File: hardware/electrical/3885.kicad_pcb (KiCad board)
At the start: 4 copper layers, 33 x 77 mm, 112 parts, among them J1 USB_B_Micro, J2 TC2030, J3 Micro_SD_Card_Det1, J4 JST-PH, J5 FFC, Q1 AO3400A, Q2 AO3400A, Q3 AO3401A, Q4 AO3401A, Q5 2N7002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

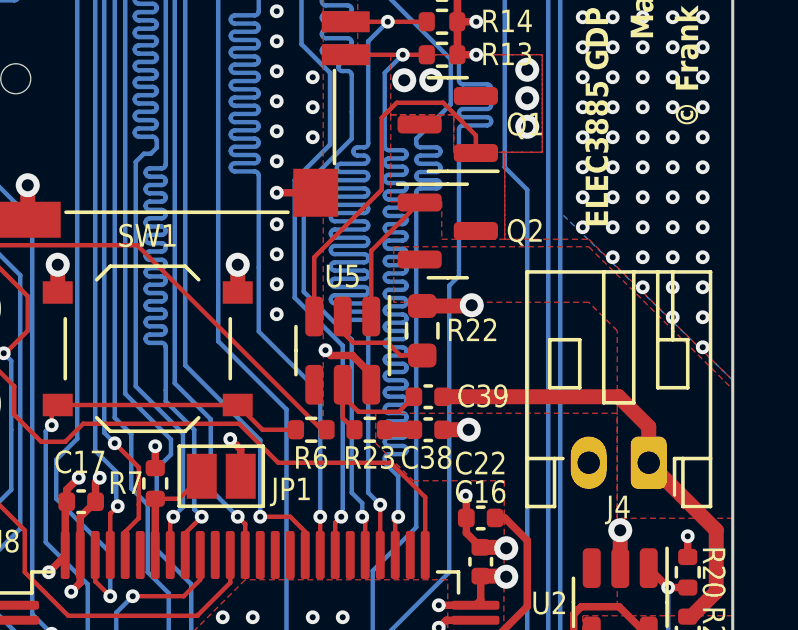
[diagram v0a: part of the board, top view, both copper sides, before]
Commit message: Implement James' recommendations
* Move R22 GND via out of -BATT fill
* Remove TP1 from schematic
* Remove TP2 from schematic
* Remove JP2 from schematic
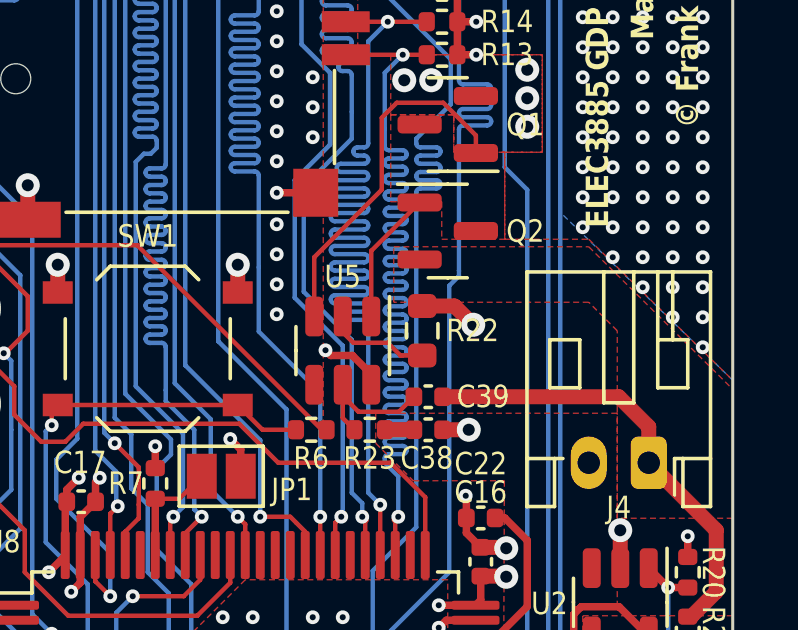
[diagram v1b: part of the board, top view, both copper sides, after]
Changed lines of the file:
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@@
     (property "ki_description" "USB Micro Type B connector")
     (property "ki_keywords" "connector USB micro")
-    (attr smd exclude_from_pos_files exclude_from_bom)
+    (attr smd exclude_from_pos_files)
     (fp_text reference "J1" (at -3.9 2.75 unlocked) (layer "F.SilkS")
         (effects (font (size 0.75 0.65) (thickness 0.12)) (justify right bottom))
@@
     (property "ki_description" "Generic connector, single row, 01x02, script generated")
     (property "ki_keywords" "connector")
-    (attr through_hole exclude_from_pos_files exclude_from_bom)
+    (attr through_hole exclude_from_pos_files)
     (fp_text reference "J4" (at 1 -1.5 unlocked) (layer "F.SilkS")
         (effects (font (size 0.75 0.65) (thickness 0.12)))
@@
     (tags "SMD SMT SPST EVQPUK EVQPUB")
     (property "LCSC Part #" "C2762970")
-    (property "Mfr" "PANASONIC")
+    (property "Mfr" "G-Switch")
     (property "Mfr. Part #" "GT-TC018B-H0375-L1")
     (property "Sheetfile" "mcu.kicad_sch")
@@
   (segment (start 150.95 76.21) (end 151 76.26) (width 0.5) (layer "F.Cu") (net 1))
   (segment (start 143.02 127.45) (end 143.02 129.1) (width 0.5) (layer "F.Cu") (net 1))
-  (segment (start 156.3 102.1) (end 156.275 102.125) (width 0.5) (layer "F.Cu") (net 1))
   (segment (start 136.25 138.16) (end 135.36 138.16) (width 0.5) (layer "F.Cu") (net 1))
   (segment (start 134.89 134.75) (end 134.25 134.75) (width 0.25) (layer "F.Cu") (net 1))
+  (segment (start 155.725 102.125) (end 154.65 102.125) (width 0.5) (layer "F.Cu") (net 1))
   (segment (start 156.12 109.19) (end 156.12 108.47) (width 0.25) (layer "F.Cu") (net 1))
   (segment (start 161.17 131.3) (end 160.3 131.3) (width 0.5) (layer "F.Cu") (net 1))
@@
   (segment (start 161.95 79.75) (end 158.98 79.75) (width 0.5) (layer "F.Cu") (net 1))
   (segment (start 138.27 119.53) (end 138.25 119.55) (width 0.25) (layer "F.Cu") (net 1))
-  (segment (start 156.275 102.125) (end 154.65 102.125) (width 0.5) (layer "F.Cu") (net 1))
   (segment (start 137.82 72.52) (end 137.8 72.5) (width 0.5) (layer "F.Cu") (net 1))
   (segment (start 161.95 76.75) (end 163.04 76.75) (width 0.5) (layer "F.Cu") (net 1))
@@
   (segment (start 143 126.85) (end 143 127.43) (width 0.25) (layer "F.Cu") (net 1))
   (segment (start 151.6 103.775) (end 151.425 103.6) (width 0.25) (layer "F.Cu") (net 1))
+  (segment (start 156.35 102.75) (end 155.725 102.125) (width 0.5) (layer "F.Cu") (net 1))
   (segment (start 138.27 114.6) (end 138.27 113.6) (width 0.25) (layer "F.Cu") (net 1))
   (segment (start 151.4 136.8) (end 150.35 136.8) (width 0.5) (layer "F.Cu") (net 1))
@@
   (via (at 138 89.5) (size 0.46) (drill 0.2) (layers "F.Cu" "B.Cu") (net 1))
   (via (at 149 112.5) (size 0.46) (drill 0.2) (layers "F.Cu" "B.Cu") (net 1))
-  (via (at 156.3 102.1) (size 0.8) (drill 0.4) (layers "F.Cu" "B.Cu") (net 1))
+  (via (at 156.35 102.75) (size 0.8) (drill 0.4) (layers "F.Cu" "B.Cu") (net 1))
   (via (at 157.25 138.65) (size 0.8) (drill 0.4) (layers "F.Cu" "B.Cu") (net 1))
   (via (at 154 79.5) (size 0.46) (drill 0.2) (layers "F.Cu" "B.Cu") (net 1))

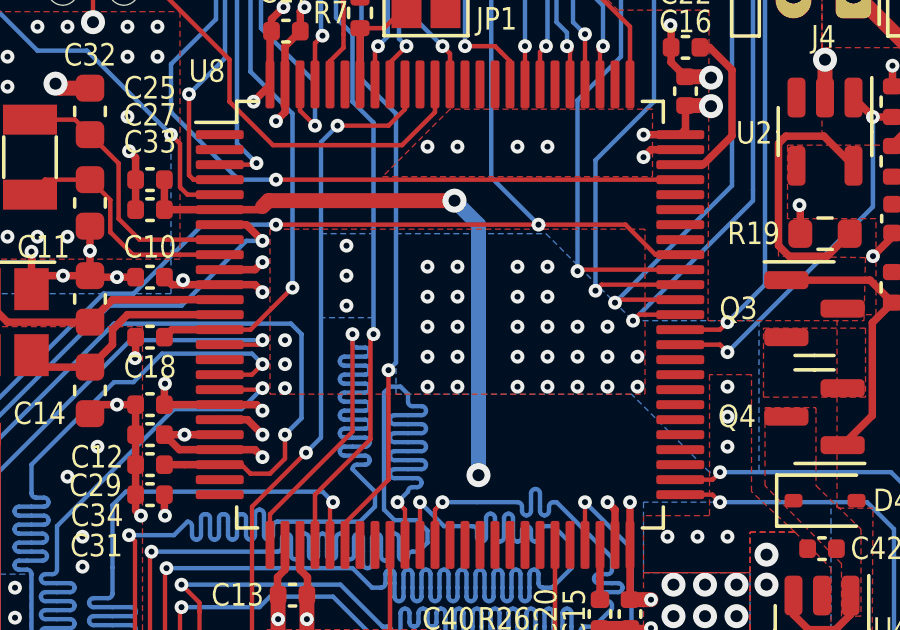
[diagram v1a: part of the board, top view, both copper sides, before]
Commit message: Add JLCPCB order number location
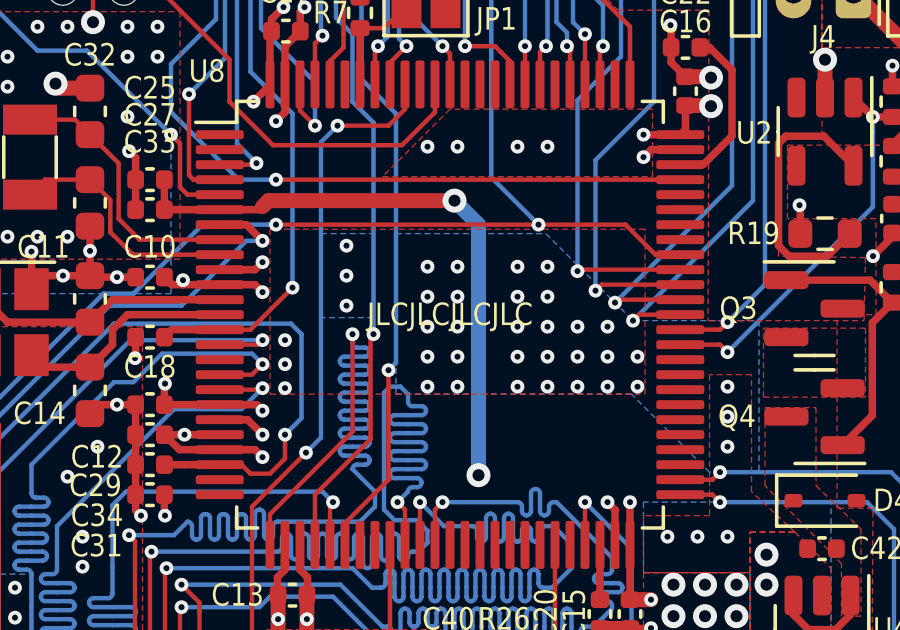
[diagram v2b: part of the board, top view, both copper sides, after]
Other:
- board text added: "JLCJLCJLCJLC"
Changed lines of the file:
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@@
   (gr_line (start 162.5 143.5) (end 134.5 143.5)
     (stroke (width 0.1) (type default)) (layer "Edge.Cuts"))
+  (gr_text "JLCJLCJLCJLC" (at 148.75 118.1) (layer "F.SilkS")
+    (effects (font (size 0.75 0.65) (thickness 0.12)))
+  )
   (gr_text "© Frank Plowman 2023" (at 163.5 84.45 90) (layer "F.SilkS")
     (effects (font (size 0.75 0.65) (thickness 0.12) bold) (justify right))

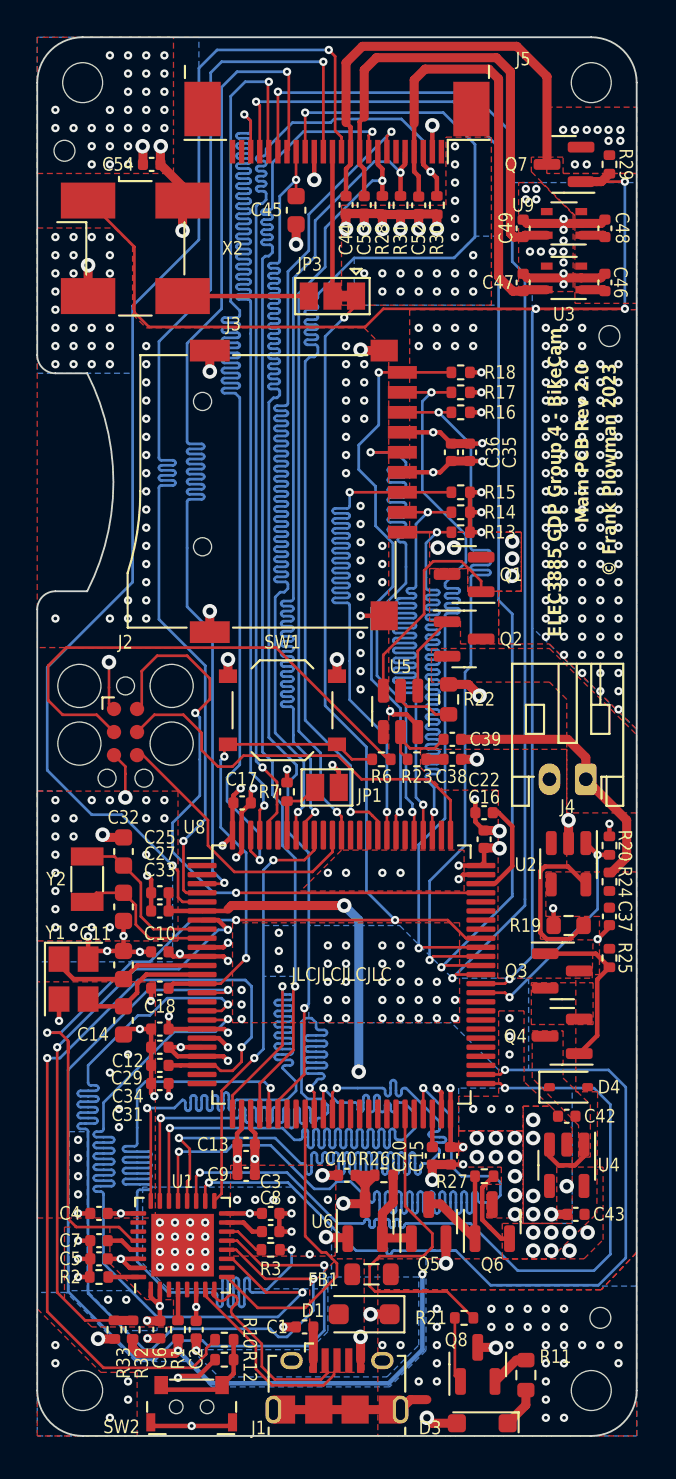
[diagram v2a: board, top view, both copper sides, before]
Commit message: Adjust part positions and rotations to match JLCPCB
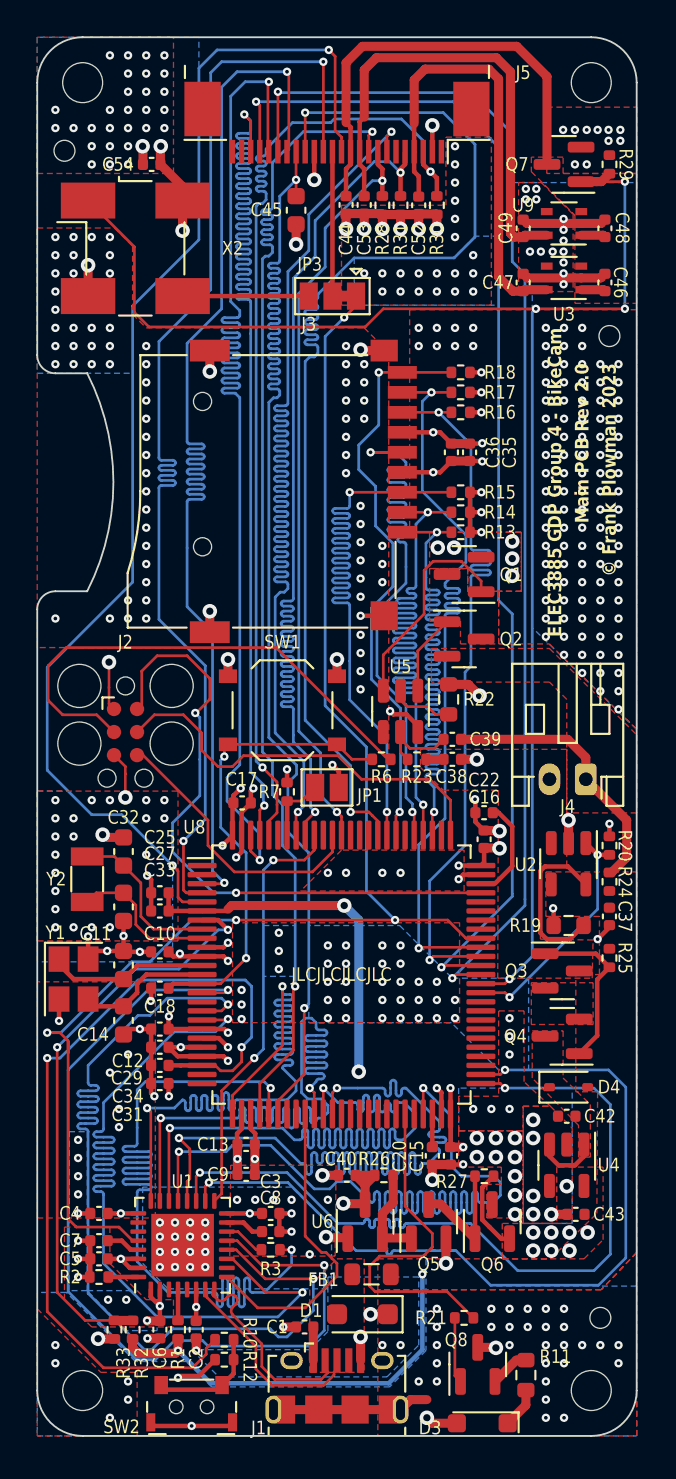
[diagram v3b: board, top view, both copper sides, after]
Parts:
- moved J3 4.15 mm to (146.9, 91.5)
- moved J5 0.75 mm to (148.5, 72.0)
- turned D1 to 0 degrees
- turned Q1 to 0 degrees
- turned Q2 to 180 degrees
- turned Q3 to 180 degrees
- turned Q4 to 0 degrees
- turned Q5 to -90 degrees
- turned Q6 to -90 degrees
- turned Q7 to 0 degrees
- turned Q8 to -90 degrees
- turned U1 to 0 degrees
- turned U2 to 180 degrees
- turned U3 to 90 degrees
- turned U4 to 180 degrees
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
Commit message: Final PCB tweaks
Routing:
- net SYS_JTDO-SWO: track 15.6 -> 39.8 mm
- net SYS_JTCK-SWCLK: track 22.6 -> 40.0 mm
- net NRST: track 28.1 -> 38.1 mm
- net SYS_JTMS-SWDIO: track 35.3 -> 36.9 mm
- net GND: vias 443 -> 442

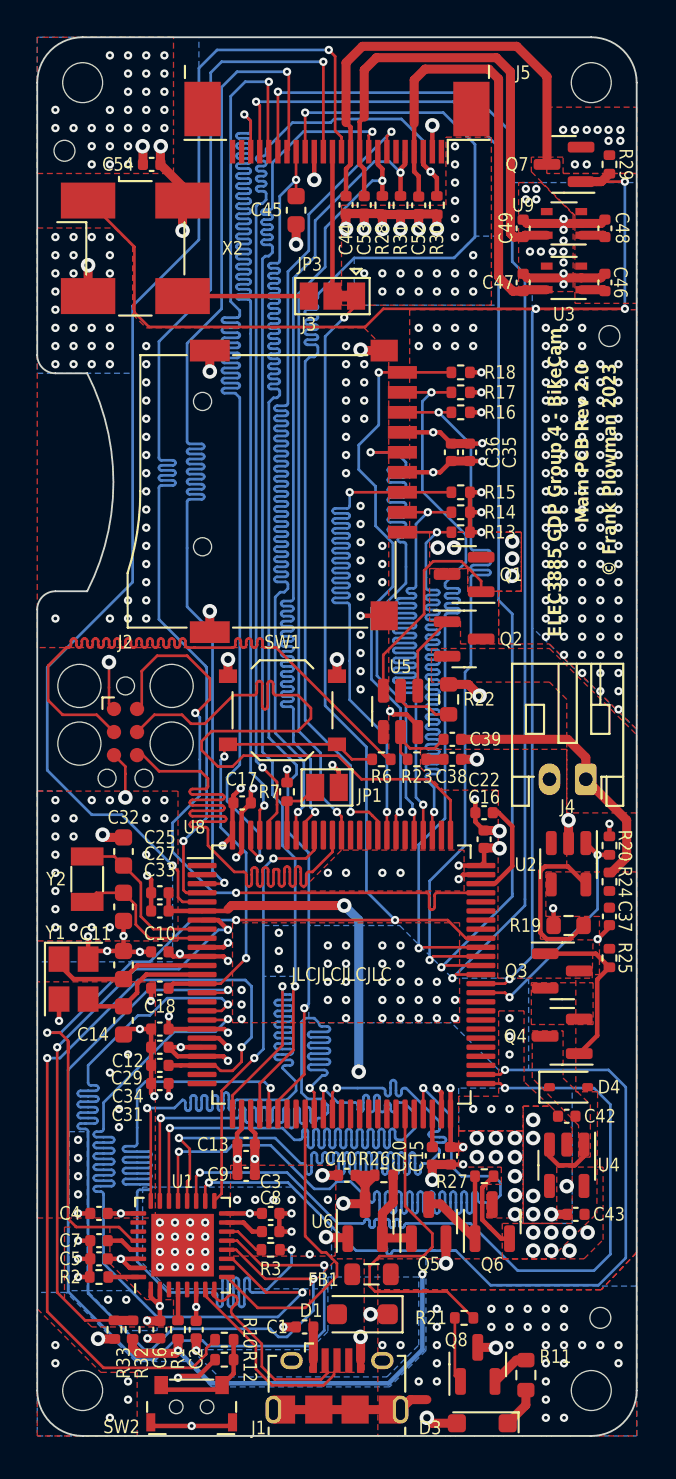
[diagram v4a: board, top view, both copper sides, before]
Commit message: Make design rules more conservative
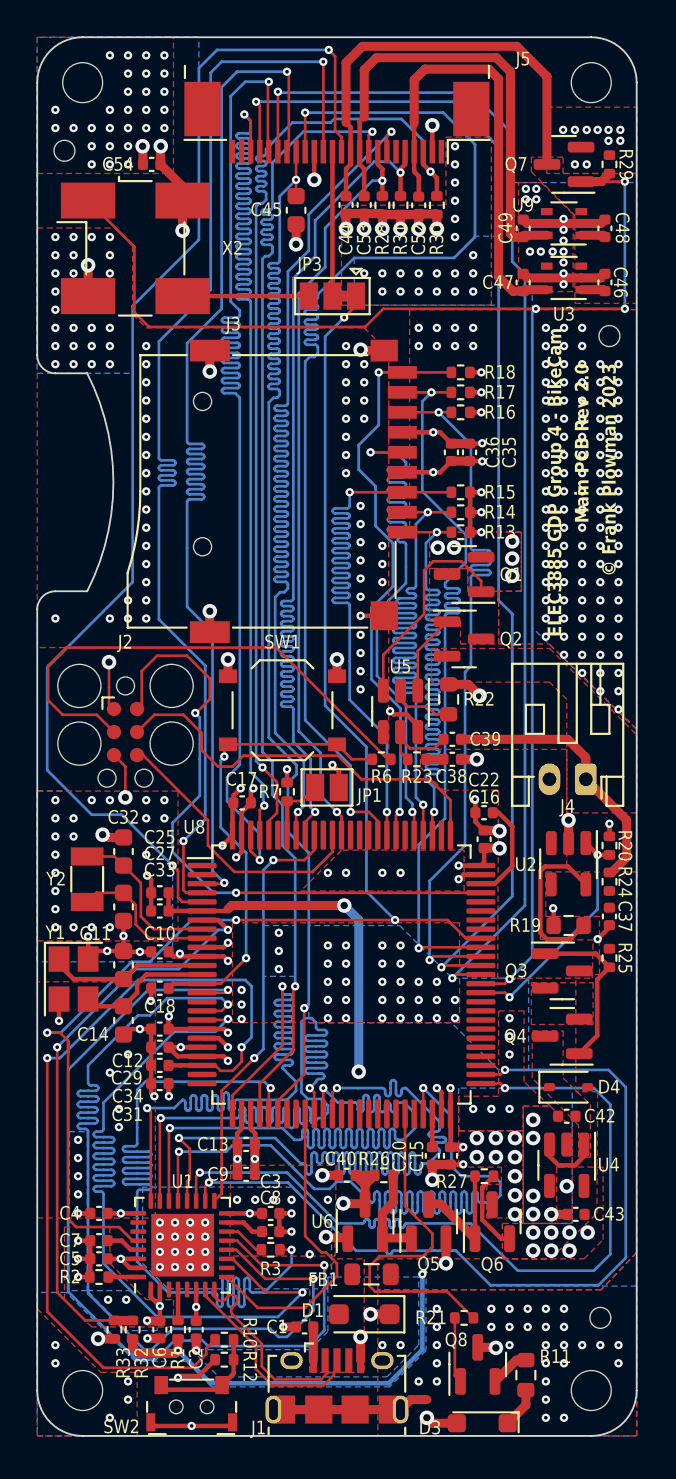
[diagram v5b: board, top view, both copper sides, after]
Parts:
- moved J3 4.15 mm to (142.8, 91.5)
- moved J5 0.75 mm to (148.5, 71.2)
- turned D1 to 180 degrees
- turned Q1 to 180 degrees
- turned Q2 to 0 degrees
- turned Q3 to 0 degrees
- turned Q4 to 180 degrees
- turned Q5 to 90 degrees
- turned Q6 to 90 degrees
- turned Q7 to 180 degrees
- turned Q8 to 90 degrees
- turned U1 to 90 degrees
- turned U2 to -90 degrees
- turned U3 to 180 degrees
- turned U4 to -90 degrees
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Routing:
- net SYS_JTDO-SWO: track 39.8 -> 15.6 mm
- net SYS_JTCK-SWCLK: track 40.0 -> 22.6 mm
- net NRST: track 38.1 -> 28.1 mm
- net SYS_JTMS-SWDIO: track 36.9 -> 35.3 mm
- net GND: vias 442 -> 443
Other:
- board text removed: "JLCJLCJLCJLC"

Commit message: Increase clearances to pass stricter DRC
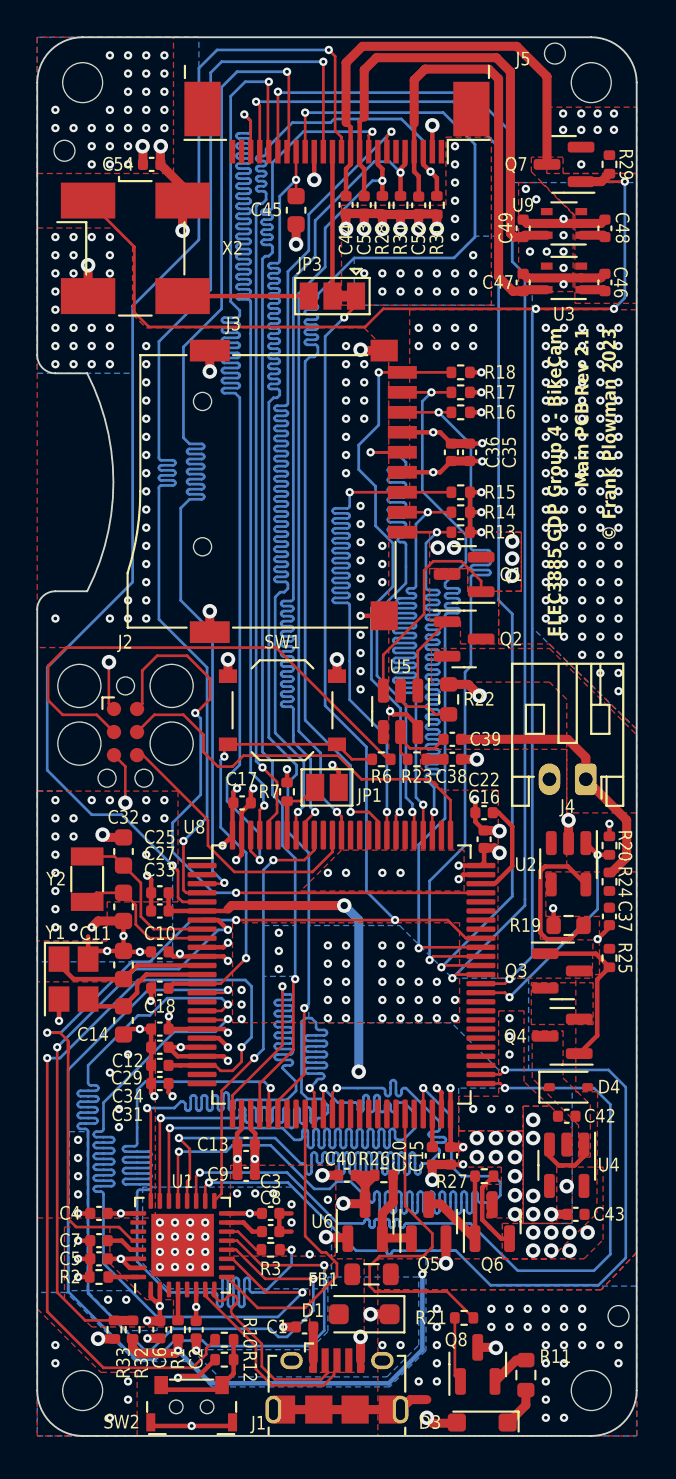
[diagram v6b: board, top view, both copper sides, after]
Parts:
- moved REF** 15.8 mm to (160.5, 67.4)
- moved REF** 1.00 mm to (164.0, 136.9)
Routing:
- net GND: track 115.8 -> 118.2 mm, vias 443 -> 435
- net VDD: track 63.8 -> 63.9 mm, vias 53 -> 52
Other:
- board text added: "Main PCB Rev 2.1"
- board text removed: "Main PCB Rev 2.0"
